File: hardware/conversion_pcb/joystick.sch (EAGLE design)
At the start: 47 parts, among them IC1 LT1168IS8, IC2 LT1168IS8, IC3 LT1168IS8, IC4 LT1168IS8, X2 22-23-2081, X3 22-23-2101

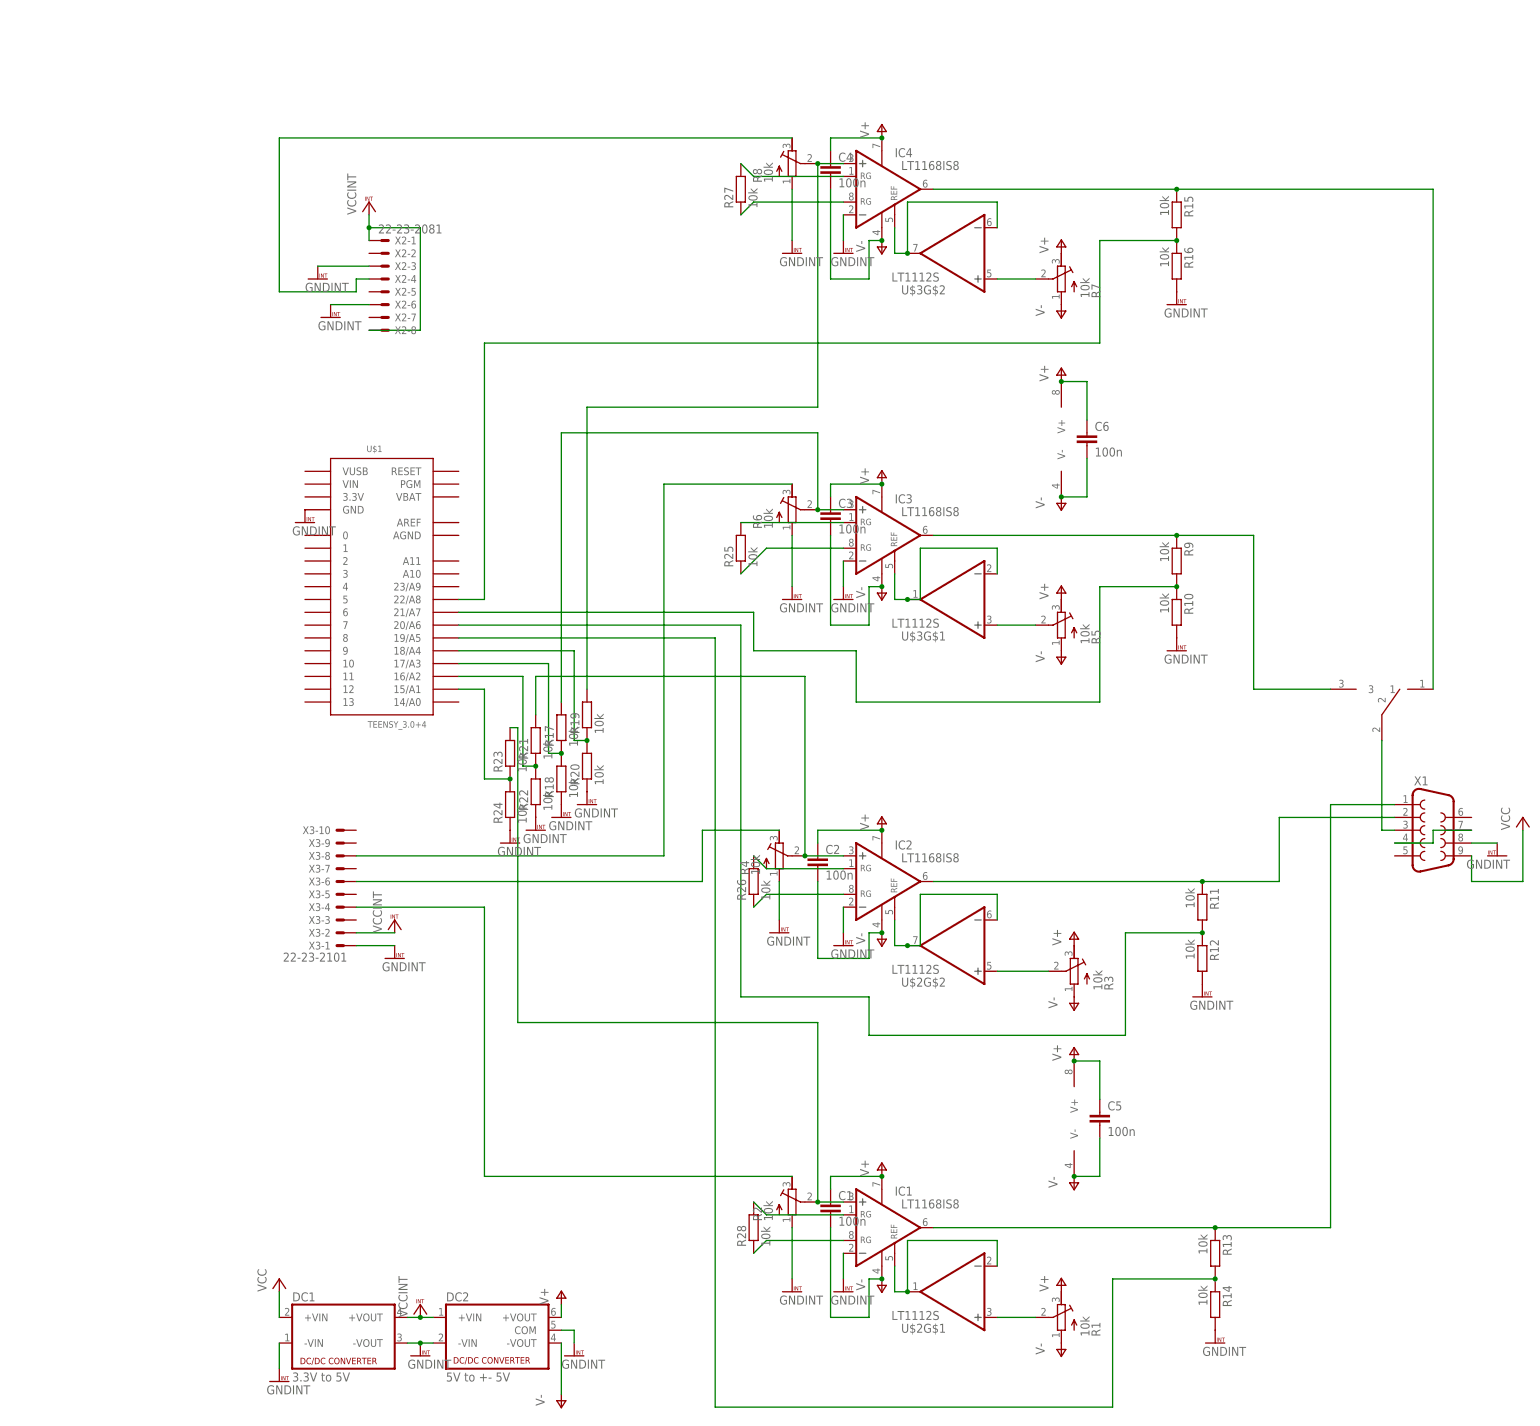
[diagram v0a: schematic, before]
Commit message: declutter circuit schematic
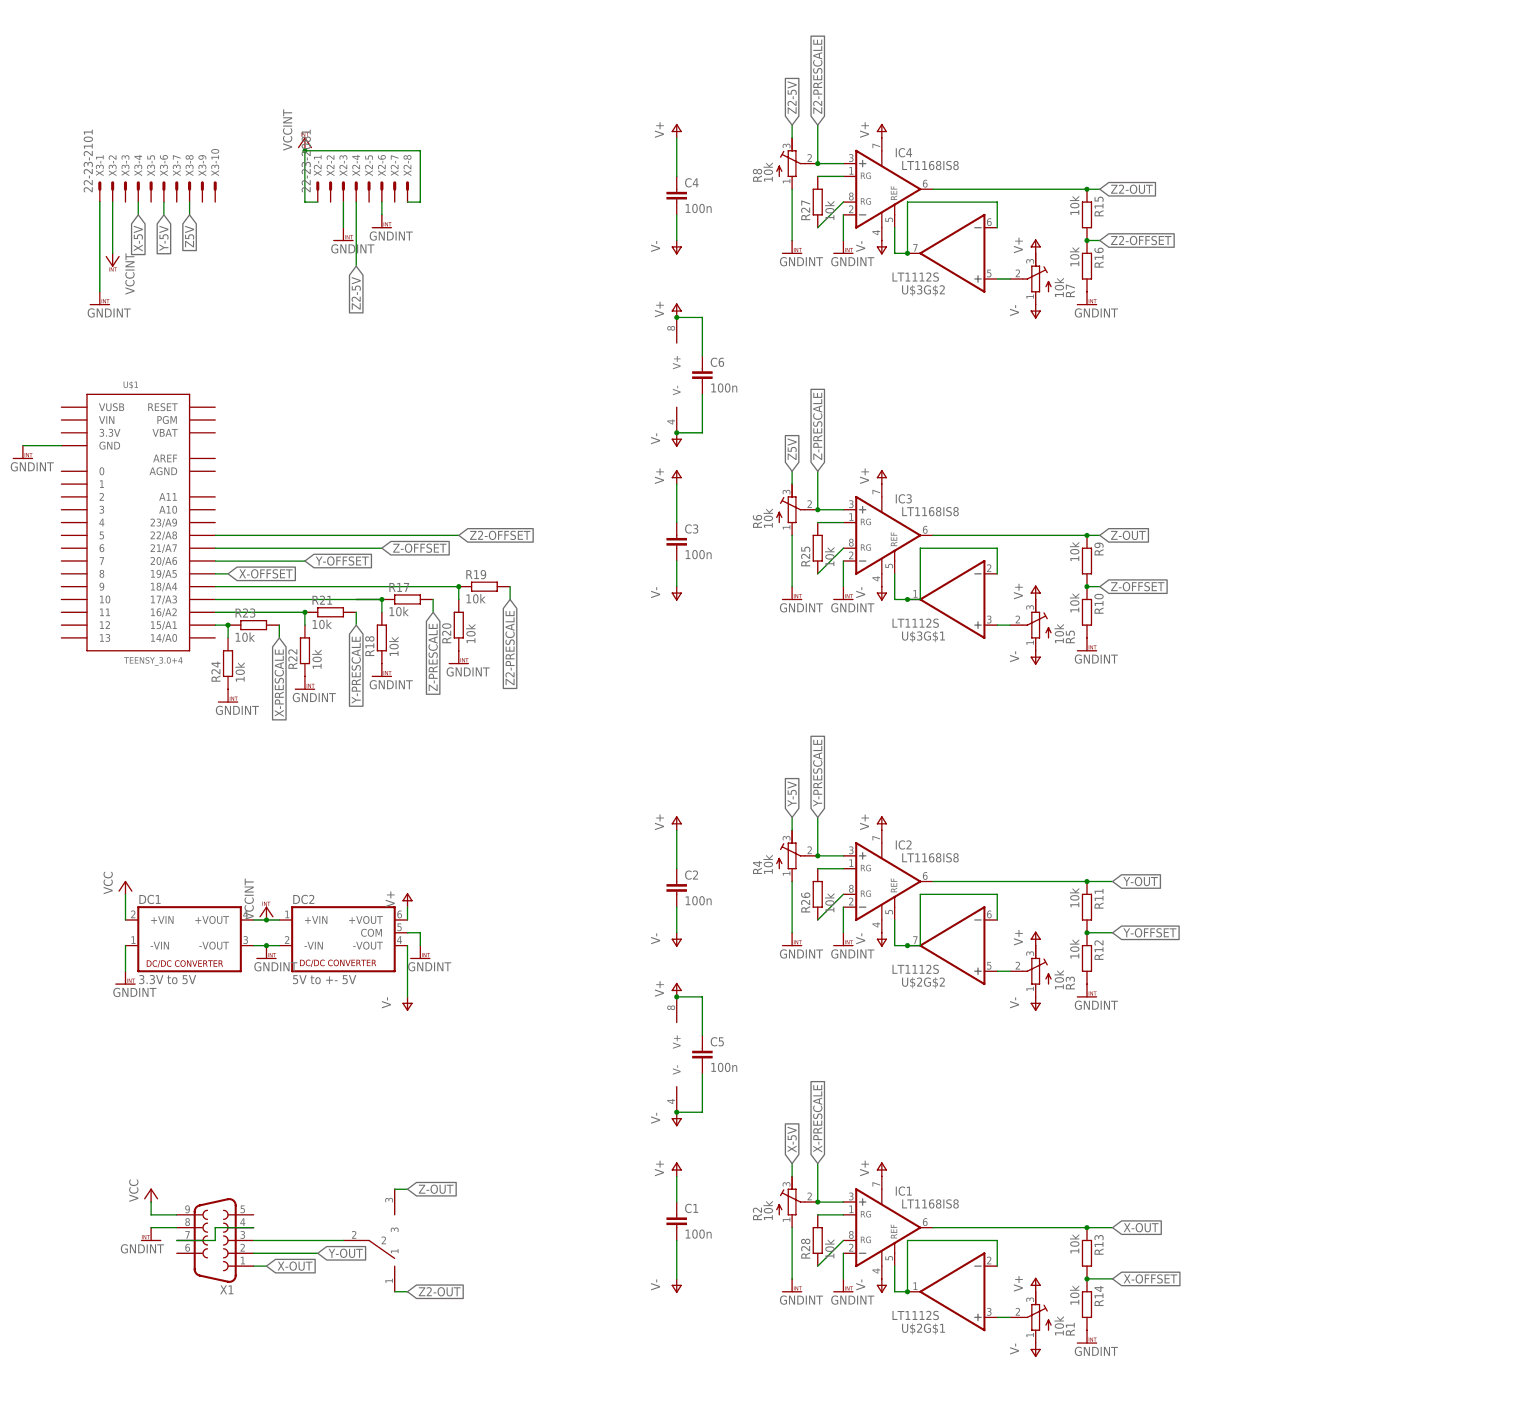
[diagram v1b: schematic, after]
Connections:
- net N$11 renamed Z2-PRESCALE
- net N$12 renamed Z2-5V
- net N$17 renamed X-OUT
- net N$18 renamed Y-OUT
- net N$19 renamed Z-OUT
- net N$2 renamed X-PRESCALE
- net N$21 renamed X-OFFSET
- net N$22 renamed Z2-OFFSET
- net N$23 renamed Z-OFFSET
- net N$24 renamed Y-OFFSET
- net N$25 renamed Z2-OUT
- net N$3 renamed X-5V
- net N$5 renamed Y-PRESCALE
- net N$6 renamed Y-5V
- net N$8 renamed Z-PRESCALE
- net N$9 renamed Z5V
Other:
- moved on the sheet: C1, C2, C3, C4, C5, C6, DC1, DC2, R1, R10, R11, R12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
